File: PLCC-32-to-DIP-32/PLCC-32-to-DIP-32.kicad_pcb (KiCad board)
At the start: 2 copper layers, 17.4 x 40.2 mm, 2 parts, among them U1 SST39SF040, U2 SST39SF040

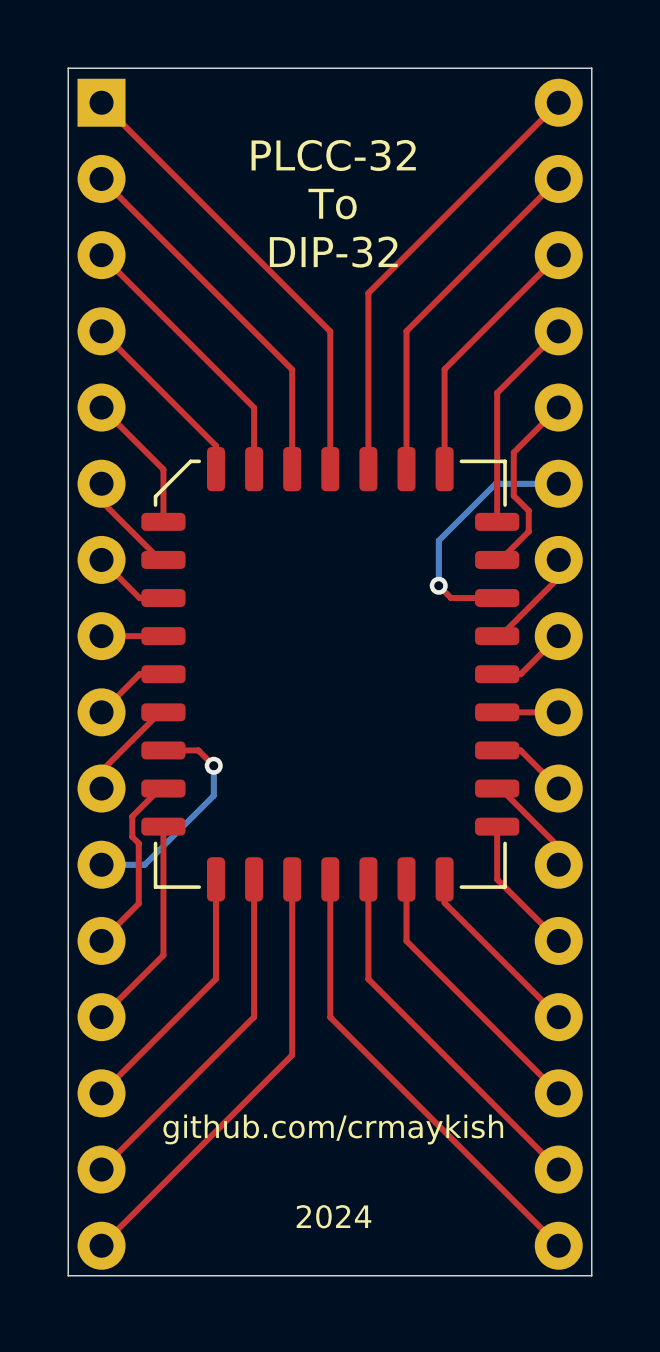
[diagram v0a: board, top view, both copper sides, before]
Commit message: Added gerbers for two adapter PCBs
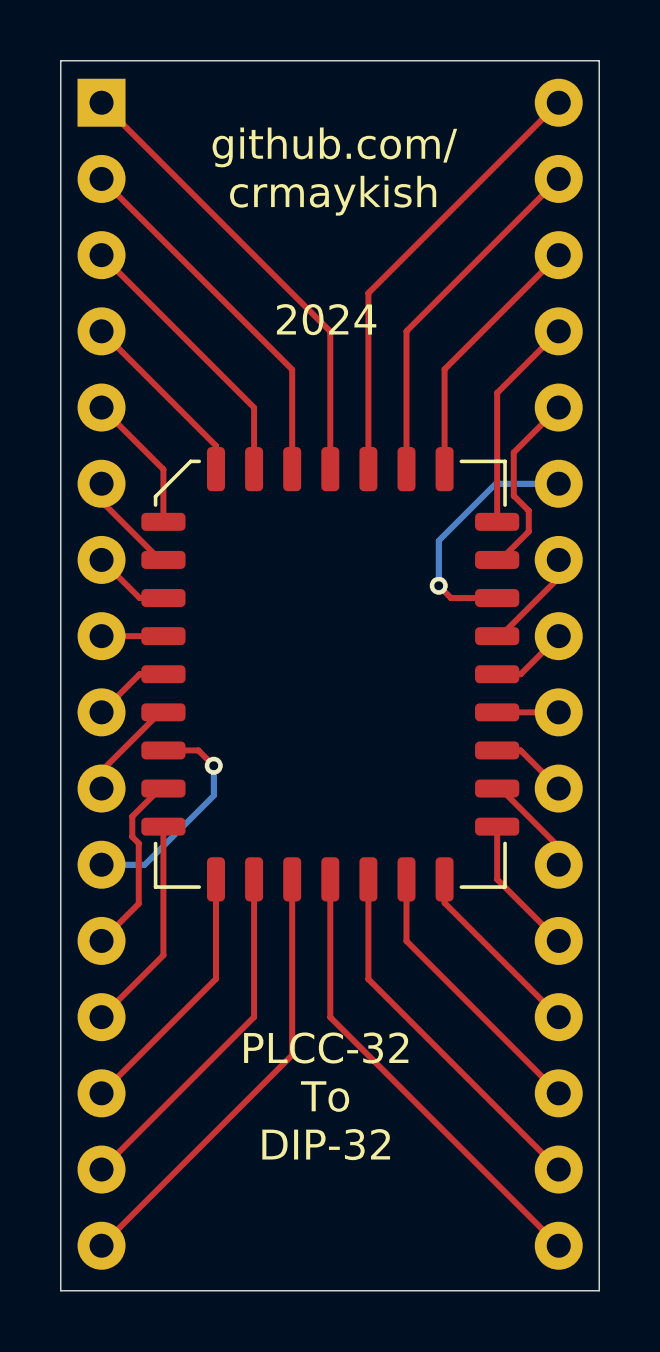
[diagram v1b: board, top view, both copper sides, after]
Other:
- board size 17.4 x 40.2 mm -> 17.9 x 41 mm
- board text added: "github.com/ crmaykish"
- board text removed: "JLCJLCJLCJLC"
- board text removed: "github.com/crmaykish"
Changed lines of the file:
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@@
 			(plot_on_all_layers_selection 0x0000000_00000000)
 			(disableapertmacros no)
-			(usegerberextensions no)
+			(usegerberextensions yes)
 			(usegerberattributes yes)
 			(usegerberadvancedattributes yes)
@@
 			(plotinvisibletext no)
 			(sketchpadsonfab no)
-			(subtractmaskfromsilk no)
+			(subtractmaskfromsilk yes)
 			(outputformat 1)
 			(mirror no)
-			(drillshape 1)
+			(drillshape 0)
 			(scaleselection 1)
-			(outputdirectory "")
+			(outputdirectory "/home/colin/Desktop/")
 		)
 	)
@@
 	)
 	(gr_rect
-		(start 132.65 67.75)
-		(end 150.1 108)
+		(start 132.4 67.5)
+		(end 150.35 108.5)
 		(stroke
 			(width 0.05)
@@
 		(layer "Edge.Cuts")
 	)
-	(gr_text "JLCJLCJLCJLC\n"
-		(at 147.5 97 90)
-		(layer "B.SilkS")
-		(effects
-			(font
-				(size 1 1)
-				(thickness 0.1)
-			)
-			(justify left bottom mirror)
-		)
-	)
 	(gr_text "PLCC-32\nTo\nDIP-32"
-		(at 141.5 74.5 0)
+		(at 141.25 104.25 0)
 		(layer "F.SilkS")
 		(effects
@@
 		)
 	)
-	(gr_text "github.com/crmaykish"
-		(at 141.5 103.5 0)
+	(gr_text "github.com/\ncrmaykish"
+		(at 141.5 72.5 0)
 		(layer "F.SilkS")
 		(effects
 			(font
-				(size 0.75 0.75)
+				(size 1 1)
 				(thickness 0.15)
 			)
@@
 	)
 	(gr_text "2024\n"
-		(at 141.5 106.5 0)
+		(at 141.25 76.75 0)
 		(layer "F.SilkS")
 		(effects
 			(font
-				(size 0.75 0.75)
+				(size 1 1)
 				(thickness 0.15)
 			)
